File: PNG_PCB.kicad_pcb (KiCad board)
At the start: 2 copper layers, 128.5 x 111 mm, 109 parts, among them J1 screw terminal, J10 screw terminal, J11 screw terminal, J12 screw terminal, J13 screw terminal, J14 screw terminal, J15 screw terminal, J16 screw terminal, J17 screw terminal, J18 screw terminal, J19 screw terminal, J2 screw terminal, J20 screw terminal, J21 screw terminal, J22 screw terminal, J23 screw terminal, J24 screw terminal, J25 screw terminal, J26 screw terminal, J27 screw terminal, J28 screw terminal, J29 screw terminal, J3 screw terminal, J30 screw terminal, J4 screw terminal, J5 screw terminal, J6 screw terminal, J7 screw terminal, J8 screw terminal, J9 screw terminal, U1 Teensy4.1, U2 Mux, U3 MCP6004, U4 Mux, U5 Mux, U6 MCP6004, U7 Mux, U8 Mux, U9 MCP6004

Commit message: changed connector verbage
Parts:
- J1, J10, J11, J12, J13, J14, J15, J16, J17, J18, J19, J2, J20, J21, J22, J23, J24, J25, J26, J27, J28, J29, J3, J30, J4, J5, J6, J7, J8, J9: value screw terminal -> connector
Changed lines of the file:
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@@
       (effects (font (size 1 1) (thickness 0.15)))
     )
-    (fp_text value "screw terminal" (at 0 2.56) (layer F.Fab)
+    (fp_text value connector (at 0 2.56) (layer F.Fab)
       (effects (font (size 1 1) (thickness 0.15)))
     )
@@
       (effects (font (size 1 1) (thickness 0.15)))
     )
-    (fp_text value "screw terminal" (at 0 2.56) (layer F.Fab)
+    (fp_text value connector (at 0 2.56) (layer F.Fab)
       (effects (font (size 1 1) (thickness 0.15)))
     )
@@
       (effects (font (size 1 1) (thickness 0.15)))
     )
-    (fp_text value "screw terminal" (at 0 2.56) (layer F.Fab)
+    (fp_text value connector (at 0 2.56) (layer F.Fab)
       (effects (font (size 1 1) (thickness 0.15)))
     )
@@
       (effects (font (size 1 1) (thickness 0.15)))
     )
-    (fp_text value "screw terminal" (at 0 2.56) (layer F.Fab)
+    (fp_text value connector (at 0 2.56) (layer F.Fab)
       (effects (font (size 1 1) (thickness 0.15)))
     )
@@
       (effects (font (size 1 1) (thickness 0.15)))
     )
-    (fp_text value "screw terminal" (at 0 2.56) (layer F.Fab)
+    (fp_text value connector (at 0 2.56) (layer F.Fab)
       (effects (font (size 1 1) (thickness 0.15)))
     )
@@
       (effects (font (size 1 1) (thickness 0.15)))
     )
-    (fp_text value "screw terminal" (at 0 2.56) (layer F.Fab)
+    (fp_text value connector (at 0 2.56) (layer F.Fab)
       (effects (font (size 1 1) (thickness 0.15)))
     )
@@
       (effects (font (size 1 1) (thickness 0.15)))
     )
-    (fp_text value "screw terminal" (at 0 2.56) (layer F.Fab)
+    (fp_text value connector (at 0 2.56) (layer F.Fab)
       (effects (font (size 1 1) (thickness 0.15)))
     )
@@
       (effects (font (size 1 1) (thickness 0.15)))
     )
-    (fp_text value "screw terminal" (at 0 2.56) (layer F.Fab)
+    (fp_text value connector (at 0 2.56) (layer F.Fab)
       (effects (font (size 1 1) (thickness 0.15)))
     )
@@
       (effects (font (size 1 1) (thickness 0.15)))
     )
-    (fp_text value "screw terminal" (at 0 2.56) (layer F.Fab)
+    (fp_text value connector (at 0 2.56) (layer F.Fab)
       (effects (font (size 1 1) (thickness 0.15)))
     )
@@
       (effects (font (size 1 1) (thickness 0.15)))
     )
-    (fp_text value "screw terminal" (at 0 2.56) (layer F.Fab)
+    (fp_text value connector (at 0 2.56) (layer F.Fab)
       (effects (font (size 1 1) (thickness 0.15)))
     )
@@
       (effects (font (size 1 1) (thickness 0.15)))
     )
-    (fp_text value "screw terminal" (at 0 2.56) (layer F.Fab)
+    (fp_text value connector (at 0 2.56) (layer F.Fab)
       (effects (font (size 1 1) (thickness 0.15)))
     )
@@
       (effects (font (size 1 1) (thickness 0.15)))
     )
-    (fp_text value "screw terminal" (at 0 2.56) (layer F.Fab)
+    (fp_text value connector (at 0 2.56) (layer F.Fab)
       (effects (font (size 1 1) (thickness 0.15)))
     )
@@
       (effects (font (size 1 1) (thickness 0.15)))
     )
-    (fp_text value "screw terminal" (at 0 2.56) (layer F.Fab)
+    (fp_text value connector (at 0 2.56) (layer F.Fab)
       (effects (font (size 1 1) (thickness 0.15)))
     )
@@
       (effects (font (size 1 1) (thickness 0.15)))
     )
-    (fp_text value "screw terminal" (at 0 2.56) (layer F.Fab)
+    (fp_text value connector (at 0 2.56) (layer F.Fab)
       (effects (font (size 1 1) (thickness 0.15)))
     )
@@
       (effects (font (size 1 1) (thickness 0.15)))
     )
-    (fp_text value "screw terminal" (at 0 2.56) (layer F.Fab)
+    (fp_text value connector (at 0 2.56) (layer F.Fab)
       (effects (font (size 1 1) (thickness 0.15)))
     )
@@
       (effects (font (size 1 1) (thickness 0.15)))
     )
-    (fp_text value "screw terminal" (at 0 2.56) (layer F.Fab)
+    (fp_text value connector (at 0 2.56) (layer F.Fab)
       (effects (font (size 1 1) (thickness 0.15)))
     )
@@
       (effects (font (size 1 1) (thickness 0.15)))
     )
-    (fp_text value "screw terminal" (at 0 2.56) (layer F.Fab)
+    (fp_text value connector (at 0 2.56) (layer F.Fab)
       (effects (font (size 1 1) (thickness 0.15)))
     )
@@
       (effects (font (size 1 1) (thickness 0.15)))
     )
-    (fp_text value "screw terminal" (at 0 2.56) (layer F.Fab)
+    (fp_text value connector (at 0 2.56) (layer F.Fab)
       (effects (font (size 1 1) (thickness 0.15)))
     )
@@
       (effects (font (size 1 1) (thickness 0.15)))
     )
-    (fp_text value "screw terminal" (at 0 2.56) (layer F.Fab)
+    (fp_text value connector (at 0 2.56) (layer F.Fab)
       (effects (font (size 1 1) (thickness 0.15)))
     )
@@
       (effects (font (size 1 1) (thickness 0.15)))
     )
-    (fp_text value "screw terminal" (at 0 2.56) (layer F.Fab)
+    (fp_text value connector (at 0 2.56) (layer F.Fab)
       (effects (font (size 1 1) (thickness 0.15)))
     )
@@
       (effects (font (size 1 1) (thickness 0.15)))
     )
-    (fp_text value "screw terminal" (at 0 2.56) (layer F.Fab)
+    (fp_text value connector (at 0 2.56) (layer F.Fab)
       (effects (font (size 1 1) (thickness 0.15)))
     )
@@
       (effects (font (size 1 1) (thickness 0.15)))
     )
-    (fp_text value "screw terminal" (at 0 2.56) (layer F.Fab)
+    (fp_text value connector (at 0 2.56) (layer F.Fab)
       (effects (font (size 1 1) (thickness 0.15)))
     )
@@
       (effects (font (size 1 1) (thickness 0.15)))
     )
-    (fp_text value "screw terminal" (at 0 2.56) (layer F.Fab)
+    (fp_text value connector (at 0 2.56) (layer F.Fab)
       (effects (font (size 1 1) (thickness 0.15)))
     )
@@
       (effects (font (size 1 1) (thickness 0.15)))
     )
-    (fp_text value "screw terminal" (at 0 2.56) (layer F.Fab)
+    (fp_text value connector (at 0 2.56) (layer F.Fab)
       (effects (font (size 1 1) (thickness 0.15)))
     )
@@
       (effects (font (size 1 1) (thickness 0.15)))
     )
-    (fp_text value "screw terminal" (at 0 2.56) (layer F.Fab)
+    (fp_text value connector (at 0 2.56) (layer F.Fab)
       (effects (font (size 1 1) (thickness 0.15)))
     )
@@
       (effects (font (size 1 1) (thickness 0.15)))
     )
-    (fp_text value "screw terminal" (at 0 2.56) (layer F.Fab)
+    (fp_text value connector (at 0 2.56) (layer F.Fab)
       (effects (font (size 1 1) (thickness 0.15)))
     )
@@
       (effects (font (size 1 1) (thickness 0.15)))
     )
-    (fp_text value "screw terminal" (at 0 2.56) (layer F.Fab)
+    (fp_text value connector (at 0 2.56) (layer F.Fab)
       (effects (font (size 1 1) (thickness 0.15)))
     )
@@
       (effects (font (size 1 1) (thickness 0.15)))
     )
-    (fp_text value "screw terminal" (at 0 2.56) (layer F.Fab)
+    (fp_text value connector (at 0 2.56) (layer F.Fab)
       (effects (font (size 1 1) (thickness 0.15)))
     )
@@
       (effects (font (size 1 1) (thickness 0.15)))
     )
-    (fp_text value "screw terminal" (at 0 2.56) (layer F.Fab)
+    (fp_text value connector (at 0 2.56) (layer F.Fab)
       (effects (font (size 1 1) (thickness 0.15)))
     )
@@
       (effects (font (size 1 1) (thickness 0.15)))
     )
-    (fp_text value "screw terminal" (at 0 2.56) (layer F.Fab)
-      (effects (font (size 1 1) (thickness 0.15)))
-    )
+    (fp_text value connector (at 0 2.56) (layer F.Fab)
+      (effects (font (size 1 1) (thickness 0.15)))
+    )

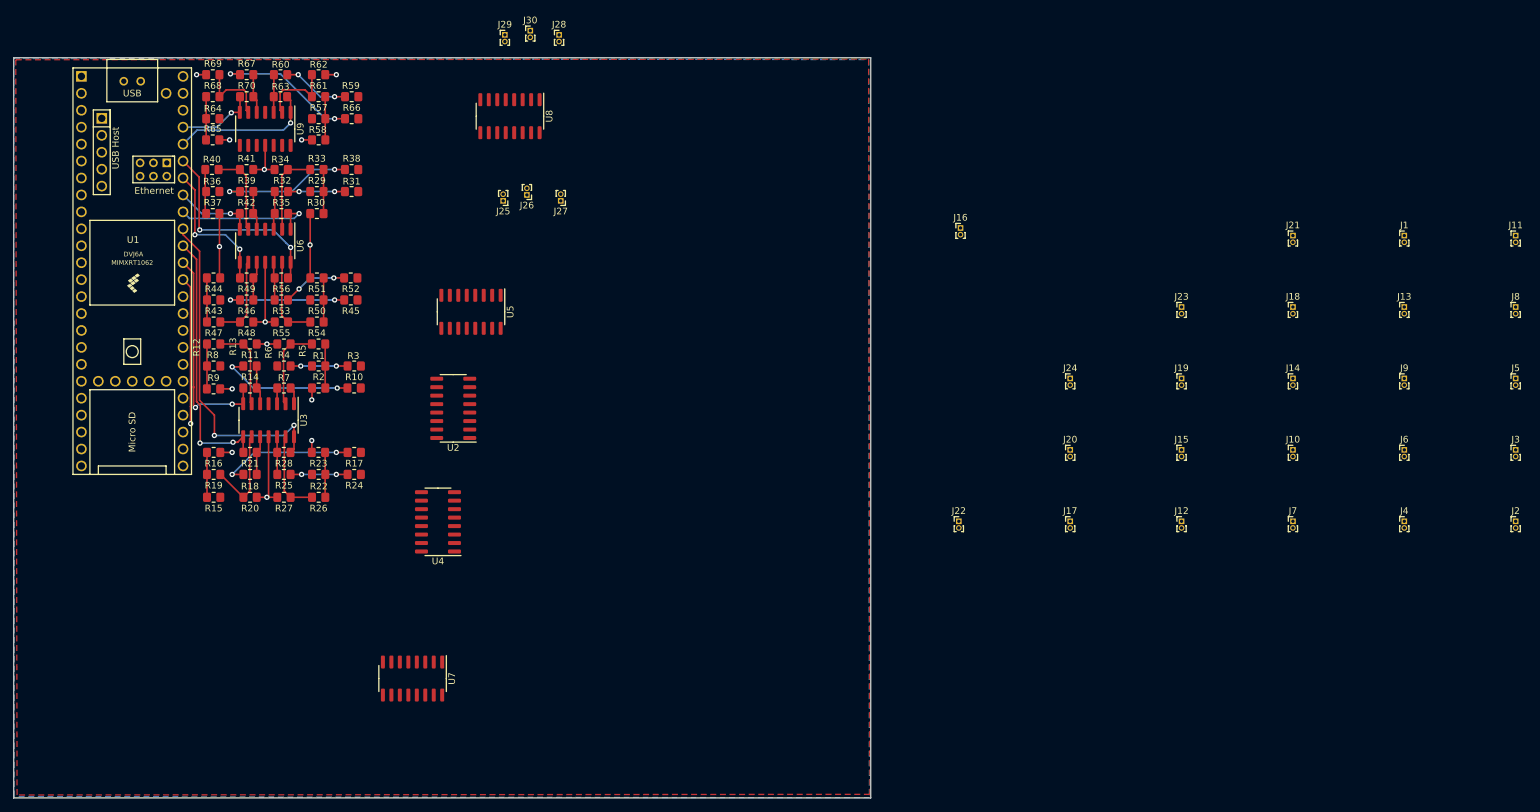
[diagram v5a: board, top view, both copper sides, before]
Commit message: routed first two mux units
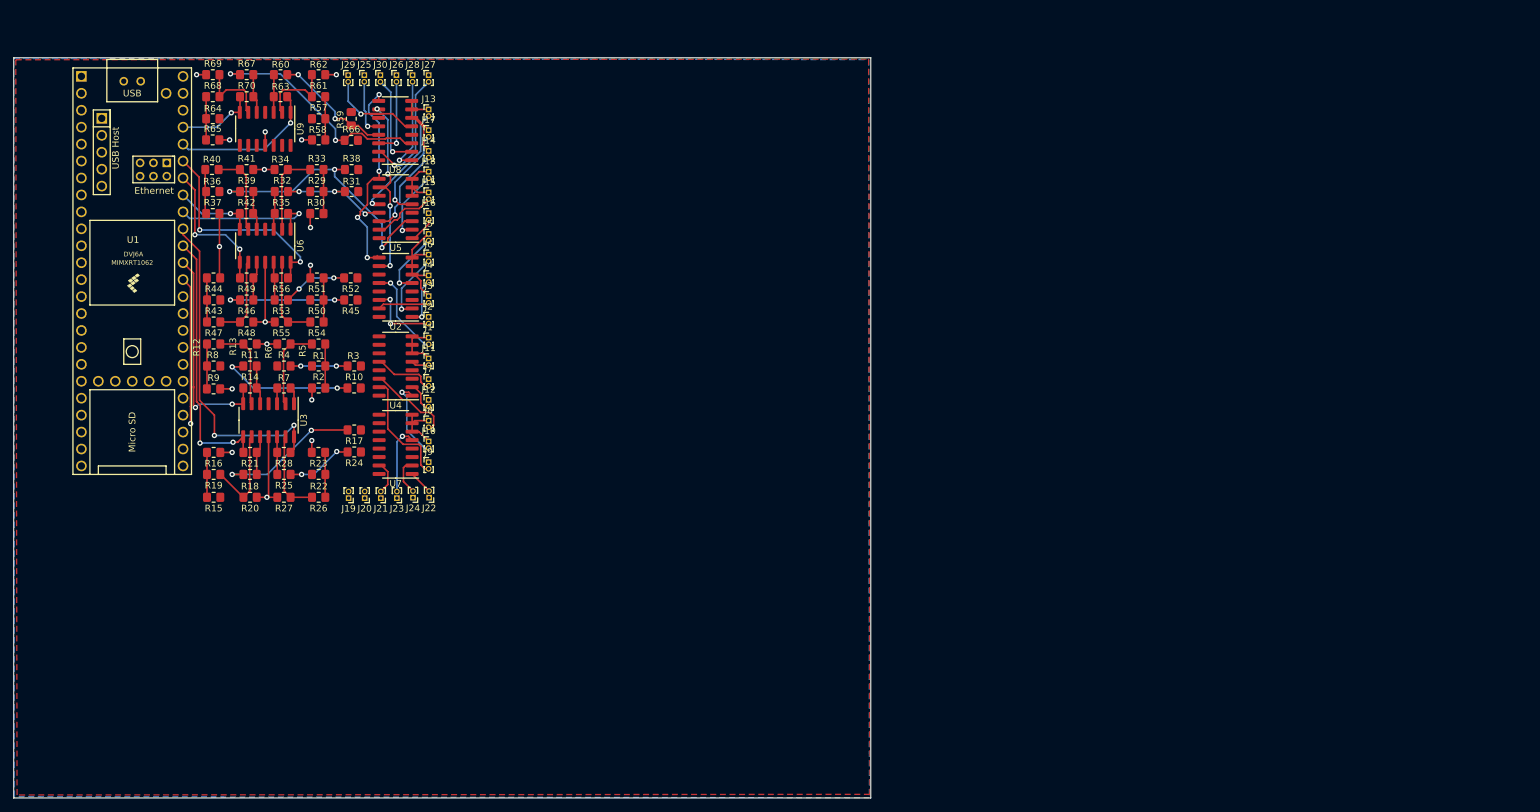
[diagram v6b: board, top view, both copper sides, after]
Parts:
- moved J2 165.9 mm to (191.8, 82.8)
- moved J3 164.6 mm to (191.8, 79.7)
- moved J5 164.4 mm to (191.8, 70.4)
- moved J11 164.0 mm to (191.8, 89.0)
- moved J8 163.9 mm to (191.8, 98.4)
- moved J4 150.9 mm to (191.8, 76.6)
- moved J13 149.3 mm to (191.8, 51.7)
- moved J6 149.2 mm to (191.8, 73.5)
- moved J1 147.1 mm to (191.8, 85.9)
- moved J9 146.8 mm to (191.8, 104.6)
- moved J21 142.3 mm to (184.6, 110.0), turned to 180 degrees
- moved J14 134.0 mm to (191.8, 57.9)
- moved J7 131.3 mm to (191.8, 92.1)
- moved J18 131.2 mm to (191.8, 61.0)
- moved J10 129.6 mm to (191.8, 101.5)
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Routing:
- net GND: track 67.4 -> 116.1 mm, vias 14 -> 16
- net /selB: track 0.00 -> 31.4 mm, vias 0 -> 4
- net /selA: track 0.00 -> 28.2 mm, vias 0 -> 4
- net /ampB1/V1: track 20.2 -> 41.4 mm, vias 2 -> 3
- net /ampA2/mux2: track 0.00 -> 18.5 mm, vias 0 -> 1
- net /ampA1/mux0: track 0.00 -> 17.8 mm, vias 0 -> 1
- net /ampC0/mux2: track 0.00 -> 17.6 mm
- net /ampB2/mux1: track 0.00 -> 16.1 mm, vias 0 -> 1
- net /ampB2/mux0: track 0.00 -> 14.4 mm, vias 0 -> 1
- net /ampB1/mux1: track 0.00 -> 14.4 mm, vias 0 -> 1
- net /ampB2/mux2: track 0.00 -> 14.1 mm, vias 0 -> 1
- net /ampA0/mux0: track 0.00 -> 13.6 mm, vias 0 -> 1
- net /ampB2/V1: track 21.4 -> 34.9 mm
- net /ampA1/mux1: track 0.00 -> 13.5 mm, vias 0 -> 1
- net /ampC0/mux1: track 0.00 -> 12.8 mm
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
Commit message: finished but have drc errors for solder holes
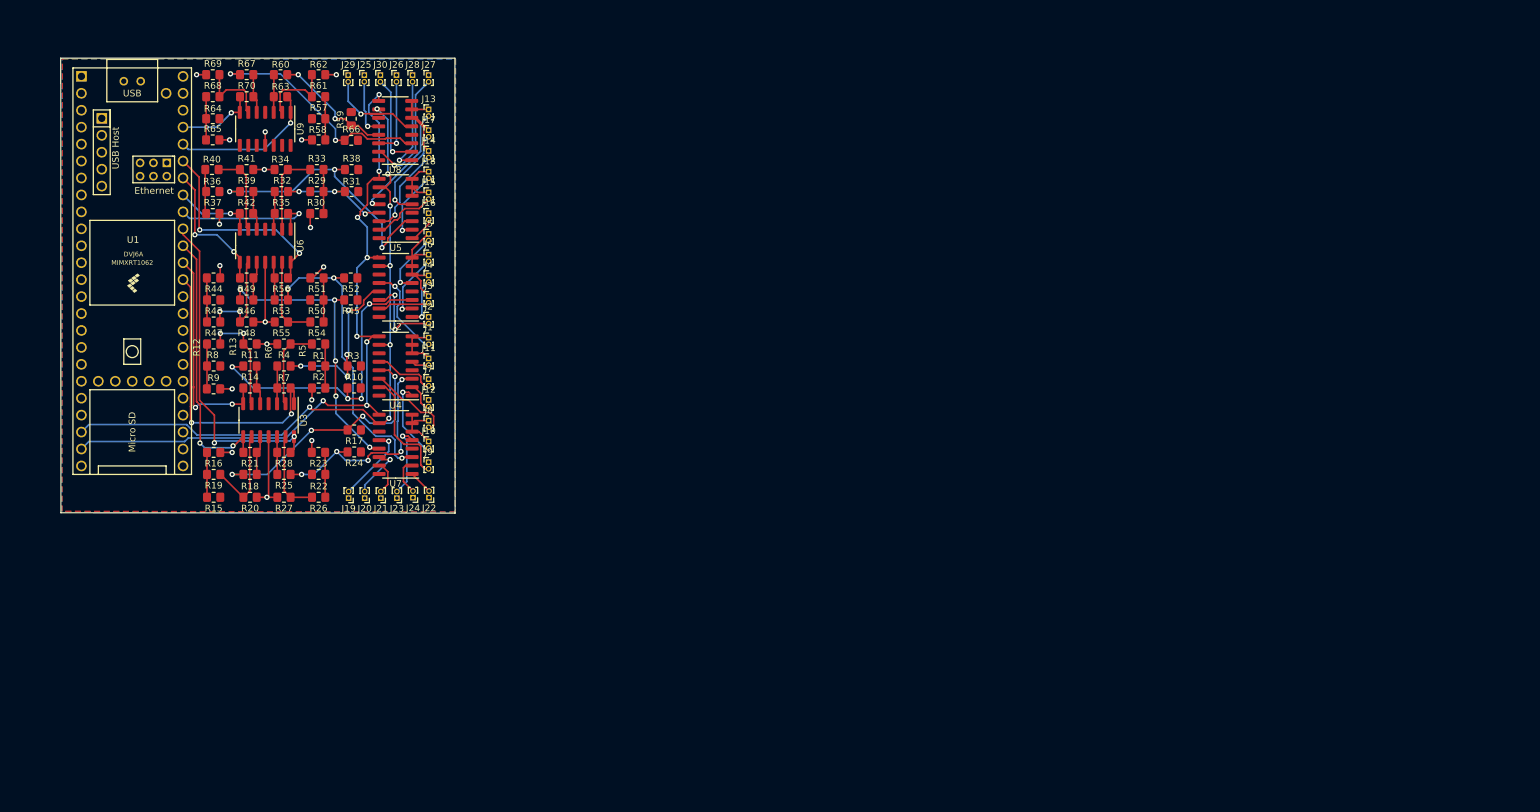
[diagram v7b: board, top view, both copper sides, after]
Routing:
- net /selB: track 31.4 -> 107.4 mm, vias 4 -> 8
- net /selA: track 28.2 -> 103.2 mm, vias 4 -> 7
- net /ampD1/V1: track 9.78 -> 45.3 mm, vias 2 -> 3
- net /ampB0/V1: track 20.3 -> 46.1 mm, vias 2 -> 4
- net /ampC1/V1: track 18.5 -> 43.6 mm, vias 2 -> 5
- net /ampD0/V1: track 9.99 -> 34.1 mm, vias 2 -> 5
- net /ADC_IN_0: track 24.7 -> 44.0 mm, vias 1 -> 2
- net /ampC0/V1: track 21.7 -> 39.6 mm, vias 2 -> 4
- net /ampA0/V1: track 8.54 -> 25.5 mm, vias 2 -> 4
- net /ampC1/mux0: track 0.00 -> 11.5 mm, vias 0 -> 1
- net /ampC1/mux1: track 0.00 -> 8.16 mm, vias 0 -> 1
- net GND: track 116.1 -> 110.6 mm, vias 16 -> 17
- net Net-(R4-Pad2): track 2.36 -> 5.67 mm
- net Net-(R47-Pad1): track 12.4 -> 15.7 mm, vias 0 -> 2
- net Net-(R12-Pad1): track 12.9 -> 16.1 mm, vias 0 -> 2
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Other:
- board size 128.5 x 111 mm -> 59.2 x 68.2 mm
